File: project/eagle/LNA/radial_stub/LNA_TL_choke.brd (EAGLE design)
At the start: 43.6 x 68.9 mm, 24 parts, among them Q1 MMBT3906LT1SMD, Q2 MMBT3906LT1SMD, Q3 SAV-541+, X1 SMA-142-0701-871/876, X2 SMA-142-0701-871/876

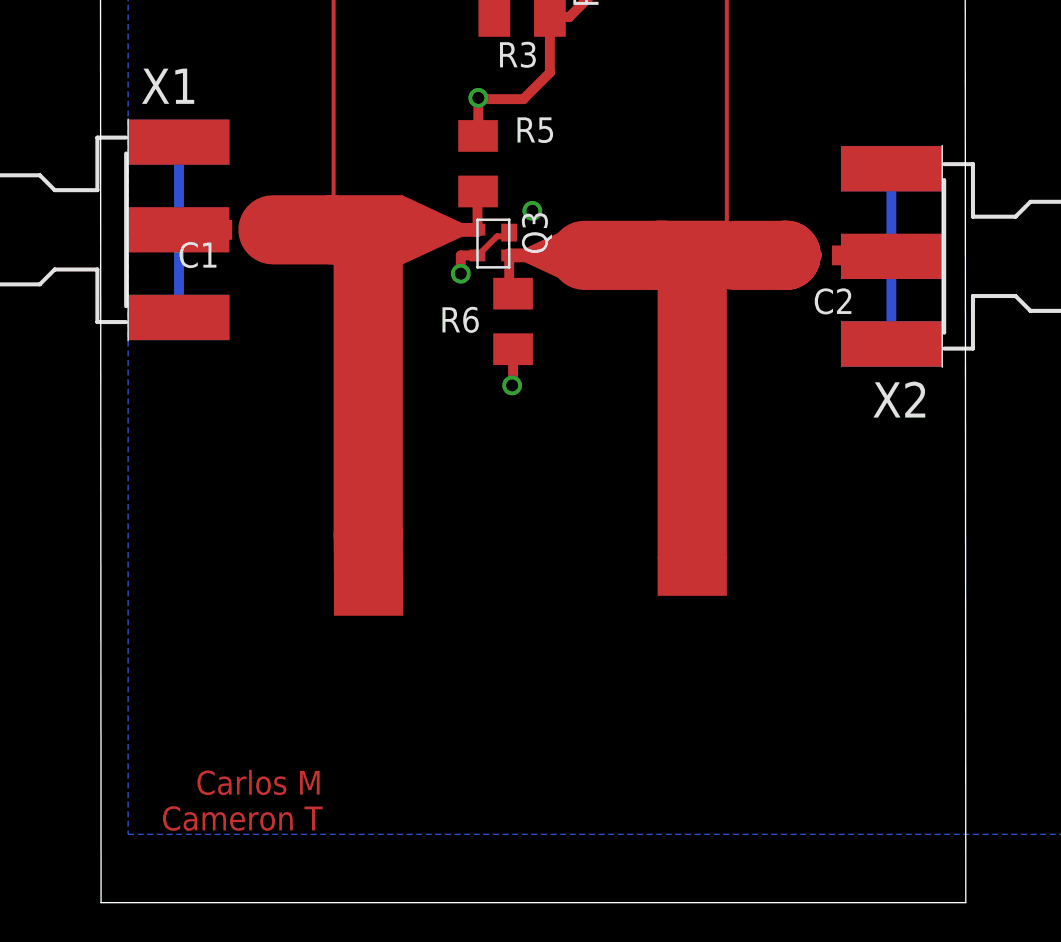
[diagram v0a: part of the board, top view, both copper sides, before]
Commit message: added measurments from camaronie v1
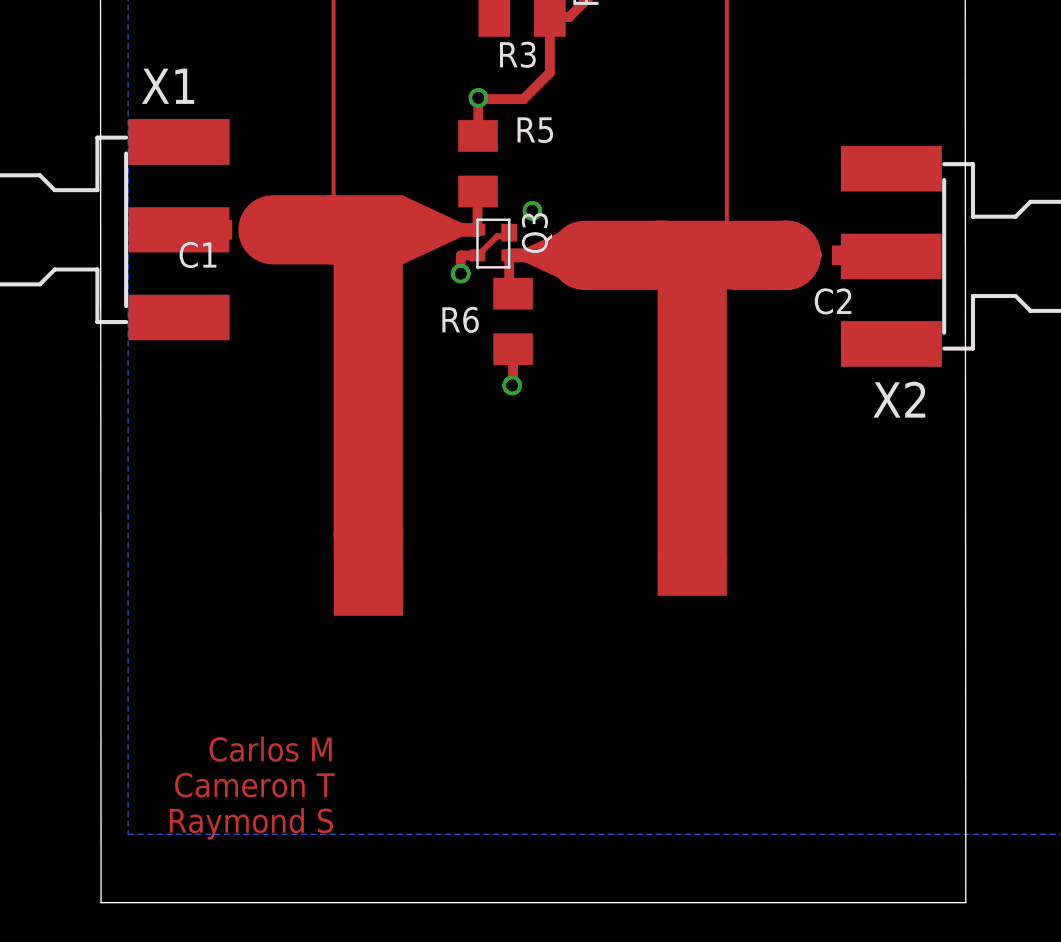
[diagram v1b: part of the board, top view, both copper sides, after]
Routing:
- net GND: track 36.7 -> 19.0 mm
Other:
- board text added: "Carlos M Cameron T Raymond S"
- board text removed: "Carlos M Cameron T"
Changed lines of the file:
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@@
 <wire x1="42.1947" y1="52.738" x2="-1.4053" y2="52.738" width="0" layer="20"/>
 <wire x1="-1.4053" y1="52.738" x2="-1.3641" y2="-16.1446" width="0" layer="20"/>
-<text x="9.8" y="-9.5" size="1.2" layer="1" font="vector" rot="R180">Carlos M
-Cameron T</text>
+<text x="10.4098" y="-7.8202" size="1.2" layer="1" font="vector" rot="R180">Carlos M
+Cameron T
+Raymond S</text>
 </plain>
 <attributes>
@@
 <wire x1="19.3636" y1="9.9334" x2="19.4098" y2="9.9334" width="0.5" layer="1"/>
 <wire x1="19.4098" y1="9.9334" x2="19.4098" y2="11.7604" width="0.5" layer="1"/>
-<wire x1="38.482" y1="20.8622" x2="38.482" y2="12.023" width="0.5" layer="16"/>
-<wire x1="2.5654" y1="22.1996" x2="2.5654" y2="13.3604" width="0.5" layer="16"/>
 <wire x1="21.2657" y1="28.512" x2="22.2455" y2="28.512" width="0.5" layer="1"/>
 <wire x1="22.2455" y1="28.512" x2="24.658" y2="30.9245" width="0.5" layer="1"/>
